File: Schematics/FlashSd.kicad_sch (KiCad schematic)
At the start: 3 parts, among them J8 Micro_SD_Card

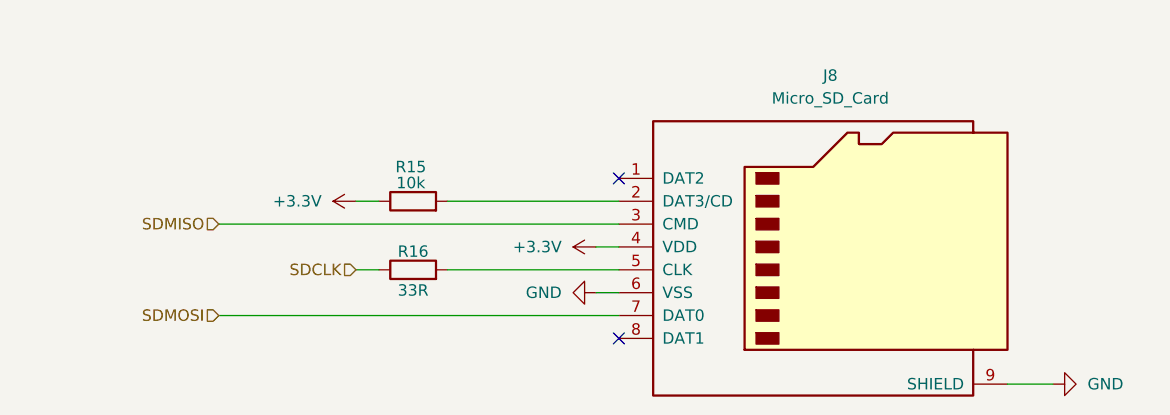
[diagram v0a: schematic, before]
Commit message: added aux pyro added reverse polarity protection re routed just need to clean up and check pin assignments
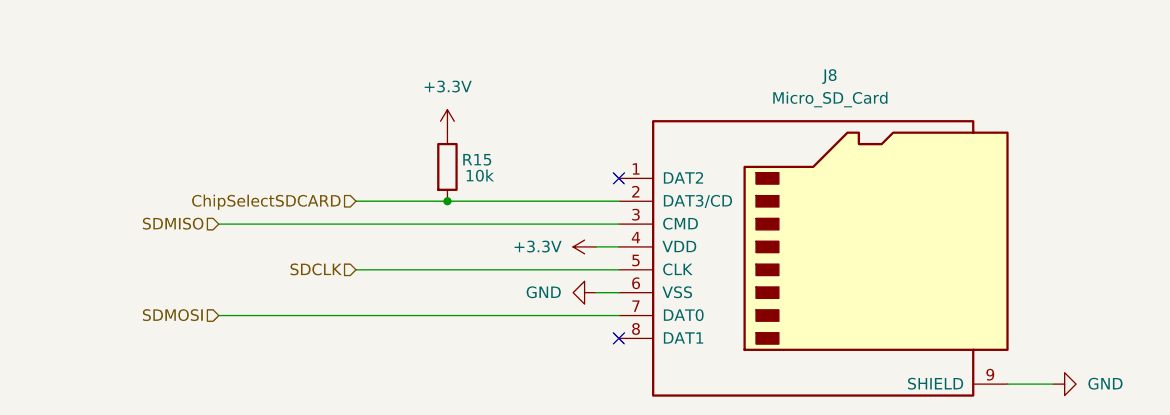
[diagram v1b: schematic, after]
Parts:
- removed R16: 33R, Resistor_SMD:R_0805_2012Metric_Pad1.20x1.40mm_HandSolder, symbol Device:R
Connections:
- net SDCLK: now also J8.5 (CLK)
- net ChipSelectSDCARD: now reaches J8.2 (DAT3/CD), R15.2
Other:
- moved on the sheet: R15

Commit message: added comments, awaiting review
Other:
- note added: "SD Card for flight telemetry logging and possible lookup tables for control systems"
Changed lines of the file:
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@@
 	(generator_version "9.0")
 	(paper "A4")
+	(text "SD Card for flight telemetry logging and possible lookup tables for control systems"
+		(exclude_from_sim no)
+		(at 143.51 68.834 0)
+		(effects
+			(font
+				(size 1.27 1.27)
+			)
+		)
+	)
 	(junction
 		(at 115.57 87.63)
@@
 	(wire
 		(pts
-			(xy 105.41 95.25) (xy 134.62 95.25)
+			(xy 90.17 95.25) (xy 134.62 95.25)
 		)
 		(stroke
@@
 	(wire
 		(pts
-			(xy 105.41 87.63) (xy 115.57 87.63)
+			(xy 90.17 87.63) (xy 115.57 87.63)
 		)
 		(stroke
@@
 	(hierarchical_label "ChipSelectSDCARD"
 		(shape input)
-		(at 105.41 87.63 180)
+		(at 90.17 87.63 180)
 		(effects
 			(font
@@
 	(hierarchical_label "SDCLK"
 		(shape input)
-		(at 105.41 95.25 180)
+		(at 90.17 95.25 180)
 		(effects
 			(font

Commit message: updated to KiCad 10.0, updated .gitignore
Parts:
- R15: LCSC C84376 -> C17414
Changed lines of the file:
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@@
 			)
 		)
-		(property "LCSC" "C84376"
+		(property "LCSC" "C17414"
 			(at 115.57 83.82 90)
 			(effects
